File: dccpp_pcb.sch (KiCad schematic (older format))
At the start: 37 parts

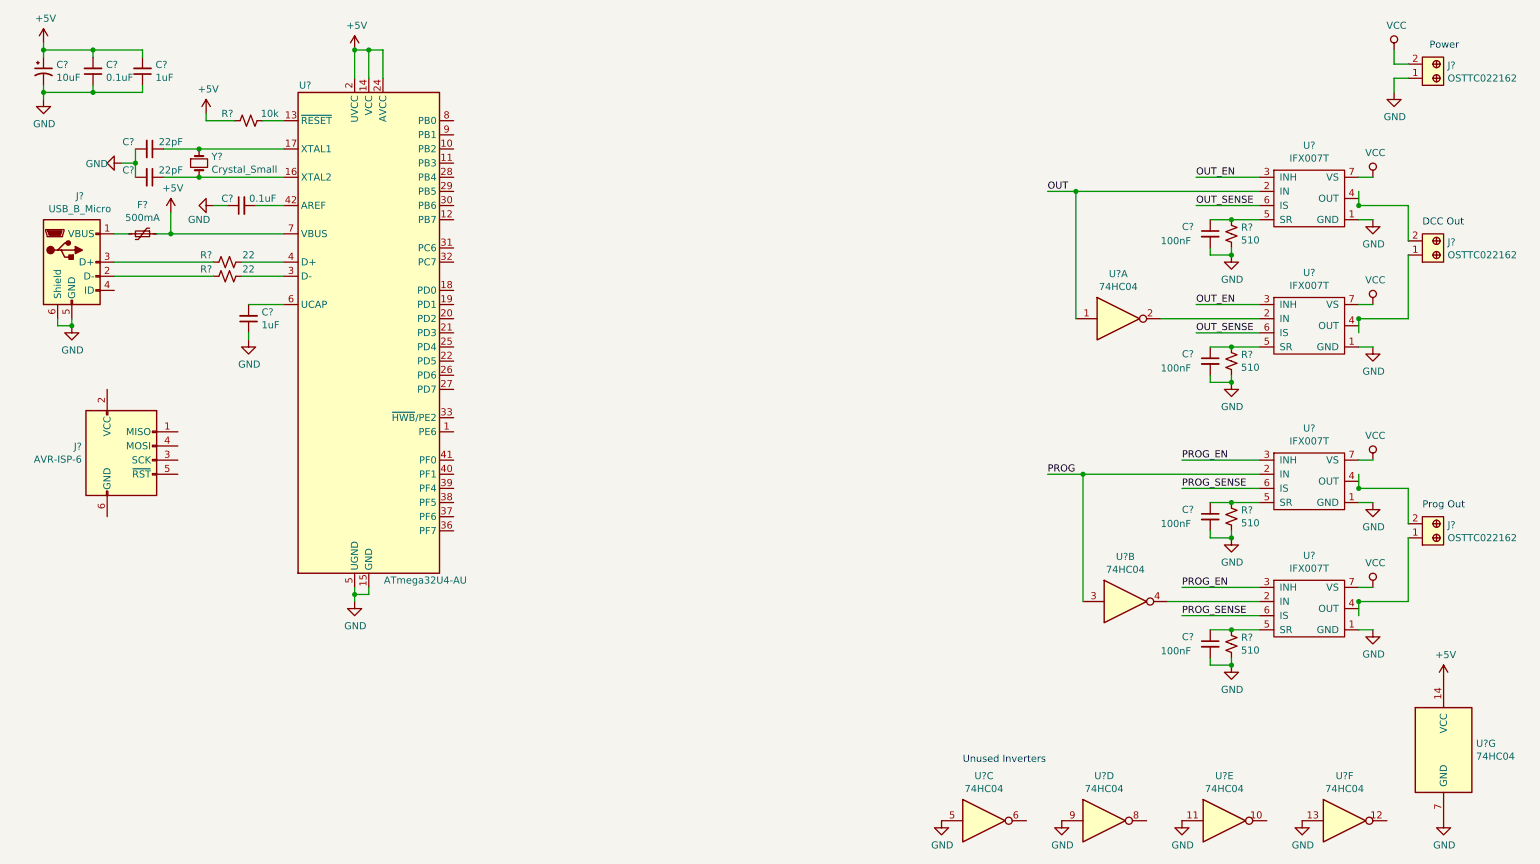
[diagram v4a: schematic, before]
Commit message: Add DCC++ pdf and current sense circuit
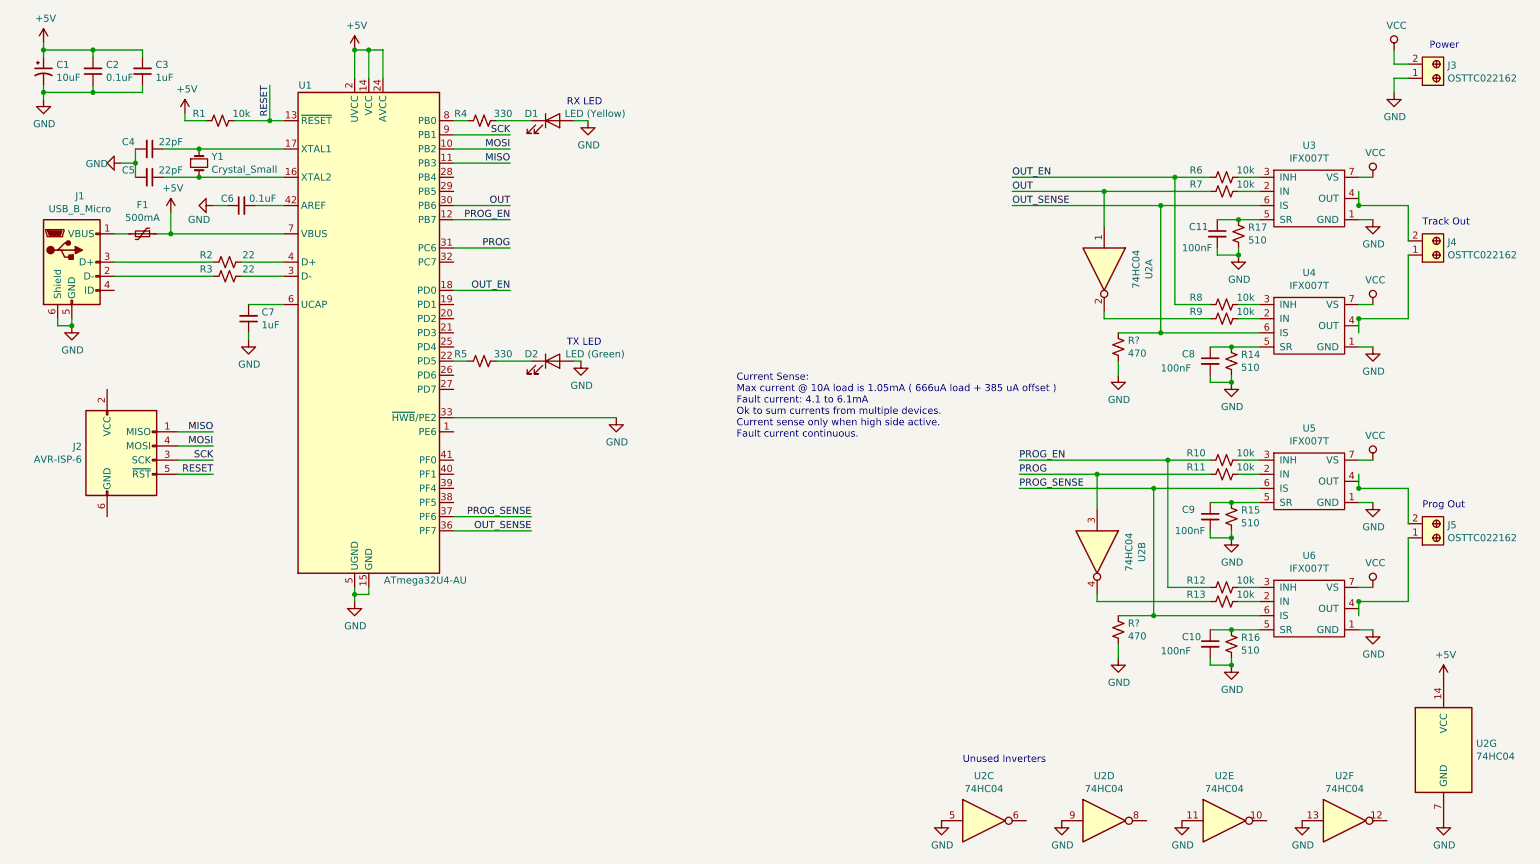
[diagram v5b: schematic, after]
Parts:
- added D1: LED (Yellow), symbol Device:LED
- added D2: LED (Green), symbol Device:LED
- added R10, R11, R12, R13, R6, R7, R8, R9: 10k, symbol Device:R_Small_US
- added R4, R5: 330, symbol Device:R_Small_US
- added R? (x2): 470, symbol Device:R_Small_US
- gave numbers to parts that had none: 31
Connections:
- net labels added: MISO, MOSI, RESET, SCK
- wire segments 106 -> 150
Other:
- note added: "Current Sense:\nMax current @ 10A load is 1.05mA ( 666uA load + 385 uA offset )\nFault current: 4.1 to 6.1mA\nOk to sum currents from multiple devices.\nCurrent sense only when high side active.\nFault current continuous."
- note added: "RX LED"
- note added: "TX LED"
- note added: "Track Out"
- note removed: "DCC Out"
- moved on the sheet: C11, R1, R17, U2A, U2B

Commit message: Fix ERC errors
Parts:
- gave numbers to parts that had none: 2
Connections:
- net +5V: now also J2.2 (VCC)
- net GND: now also J2.6 (GND)
- net D7: now reaches U1.1 (PE6)
- net D2: now reaches U1.19 (PD1)
- net D0: now reaches U1.20 (PD2)
- net D1: now reaches U1.21 (PD3)
- net D4: now reaches U1.25 (PD4)
- net D12: now reaches U1.26 (PD6)
- net D6: now reaches U1.27 (PD7)
- net D8: now reaches U1.28 (PB4)
- net D9: now reaches U1.29 (PB5)
- net D13: now reaches U1.32 (PC7)
- net A2: now reaches U1.38 (PF5)
- net A3: now reaches U1.39 (PF4)
- net A4: now reaches U1.40 (PF1)
- net A5: now reaches U1.41 (PF0)
- net at J4.1: now also U4.4 (OUT), U4.8 (OUT)
- net at J4.2: now also U3.4 (OUT), U3.8 (OUT)
- net at U5.4 (OUT), U5.8 (OUT): now also J5.2
- net at U6.4 (OUT), U6.8 (OUT): now also J5.1
- no-connect marks 0 -> 5
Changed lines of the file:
@@
 	10100 2000 10000 2000
 Wire Wire Line
-	10000 1800 10000 1900
-Wire Wire Line
-	10000 1900 10350 1900
-Connection ~ 10000 1900
-Wire Wire Line
-	10350 2250 10350 2700
-Wire Wire Line
-	10350 2700 10000 2700
-Wire Wire Line
-	10000 2700 10000 2800
-Connection ~ 10000 2700
+	10000 1850 10350 1850
+Wire Wire Line
+	10350 2250 10350 2750
+Wire Wire Line
+	10350 2750 10000 2750
 $Comp
 L dccpp:IFX007T U5
@@
 	10250 1000 10250 1100
 Wire Wire Line
-	10350 1900 10350 2150
+	10350 1850 10350 2150
 Wire Wire Line
 	10000 4900 10100 4900
@@
 	10000 3700 10100 3700
 Wire Wire Line
-	10000 3800 10000 3900
-Wire Wire Line
-	10000 3900 10350 3900
-Wire Wire Line
-	10350 3900 10350 4150
-Connection ~ 10000 3900
-Wire Wire Line
-	10350 4250 10350 4700
-Wire Wire Line
-	10350 4700 10000 4700
-Wire Wire Line
-	10000 4700 10000 4800
-Connection ~ 10000 4700
+	10000 3850 10350 3850
+Wire Wire Line
+	10350 3850 10350 4150
+Wire Wire Line
+	10350 4250 10350 4750
+Wire Wire Line
+	10350 4750 10000 4750
 Text Notes 10450 4050 0    50   ~ 0
 Prog Out
@@
 Current Sense:\nMax current @ 10A load is 1.05mA ( 666uA load + 385 uA offset )\nFault current: 4.1 to 6.1mA\nOk to sum currents from multiple devices.\nCurrent sense only when high side active.\nFault current continuous.
 $Comp
-L Device:R_Small_US R?
+L Device:R_Small_US R19
 U 1 1 5D3AA9FD
 P 8300 4900
-F 0 "R?" H 8368 4946 50  0000 L CNN
+F 0 "R19" H 8368 4946 50  0000 L CNN
 F 1 "470" H 8368 4855 50  0000 L CNN
 F 2 "" H 8300 4900 50  0001 C CNN
@@
 $EndComp
 $Comp
-L Device:R_Small_US R?
+L Device:R_Small_US R18
 U 1 1 5D3AB504
 P 8300 2900
-F 0 "R?" H 8368 2946 50  0000 L CNN
+F 0 "R18" H 8368 2946 50  0000 L CNN
 F 1 "470" H 8368 2855 50  0000 L CNN
 F 2 "" H 8300 2900 50  0001 C CNN
@@
 $EndComp
 $Comp
-L power:GND #PWR?
+L power:GND #PWR0134
 U 1 1 5D3B2373
 P 8300 3100
-F 0 "#PWR?" H 8300 2850 50  0001 C CNN
+F 0 "#PWR0134" H 8300 2850 50  0001 C CNN
 F 1 "GND" H 8305 2927 50  0000 C CNN
 F 2 "" H 8300 3100 50  0001 C CNN
@@
 $EndComp
 $Comp
-L power:GND #PWR?
+L power:GND #PWR0135
 U 1 1 5D3B27C2
 P 8300 5100
-F 0 "#PWR?" H 8300 4850 50  0001 C CNN
+F 0 "#PWR0135" H 8300 4850 50  0001 C CNN
 F 1 "GND" H 8305 4927 50  0000 C CNN
 F 2 "" H 8300 5100 50  0001 C CNN
@@
 Wire Wire Line
 	8300 5100 8300 5000
+$Comp
+L power:+5V #PWR0136
+U 1 1 5D3F86B0
+P 1150 3200
+F 0 "#PWR0136" H 1150 3050 50  0001 C CNN
+F 1 "+5V" H 1165 3373 50  0000 C CNN
+F 2 "" H 1150 3200 50  0001 C CNN
+F 3 "" H 1150 3200 50  0001 C CNN
+	1    1150 3200
+	1    0    0    -1
+$EndComp
+$Comp
+L power:GND #PWR0137
+U 1 1 5D3F8F1D
+P 1150 4100
+F 0 "#PWR0137" H 1150 3850 50  0001 C CNN
+F 1 "GND" H 1155 3927 50  0000 C CNN
+F 2 "" H 1150 4100 50  0001 C CNN
+F 3 "" H 1150 4100 50  0001 C CNN
+	1    1150 4100
+	1    0    0    -1
+$EndComp
+NoConn ~ 7650 6250
+NoConn ~ 8500 6250
+NoConn ~ 9350 6250
+NoConn ~ 10200 6250
+NoConn ~ 1200 2500
+Text Label 4000 2700 2    50   ~ 0
+D0
+Text Label 4000 2800 2    50   ~ 0
+D1
+Text Label 4000 2600 2    50   ~ 0
+D2
+Text Label 4000 2900 2    50   ~ 0
+D4
+Text Label 4000 3200 2    50   ~ 0
+D6
+Text Label 4000 3500 2    50   ~ 0
+D7
+Text Label 4000 1700 2    50   ~ 0
+D8
+Text Label 4000 1800 2    50   ~ 0
+D9
+Text Label 4000 3100 2    50   ~ 0
+D12
+Text Label 4150 4000 2    50   ~ 0
+A2
+Text Label 4150 3900 2    50   ~ 0
+A3
+Text Label 4150 3800 2    50   ~ 0
+A4
+Text Label 4150 3700 2    50   ~ 0
+A5
+Wire Wire Line
+	4150 3700 3600 3700
+Wire Wire Line
+	3600 3800 4150 3800
+Wire Wire Line
+	4150 3900 3600 3900
+Wire Wire Line
+	4150 4000 3600 4000
+Wire Wire Line
+	4000 3500 3600 3500
+Wire Wire Line
+	3600 3200 4000 3200
+Wire Wire Line
+	4000 3100 3600 3100
+Wire Wire Line
+	3600 2900 4000 2900
+Wire Wire Line
+	4000 2800 3600 2800
+Wire Wire Line
+	3600 2700 4000 2700
+Wire Wire Line
+	4000 2600 3600 2600
+Wire Wire Line
+	3600 1800 4000 1800
+Wire Wire Line
+	4000 1700 3600 1700
+Text Label 4000 2300 2    50   ~ 0
+D13
+Wire Wire Line
+	4000 2300 3600 2300
+$Comp
+L power:PWR_FLAG #FLG0101
+U 1 1 5D4E6B43
+P 1050 800
+F 0 "#FLG0101" H 1050 875 50  0001 C CNN
+F 1 "PWR_FLAG" H 1050 973 50  0000 C CNN
+F 2 "" H 1050 800 50  0001 C CNN
+F 3 "~" H 1050 800 50  0001 C CNN
+	1    1050 800
+	1    0    0    -1
+$EndComp
+$Comp
+L power:PWR_FLAG #FLG0103
+U 1 1 5D4EA9C3
+P 10250 900
+F 0 "#FLG0103" H 10250 975 50  0001 C CNN
+F 1 "PWR_FLAG" V 10250 1027 50  0000 L CNN
+F 2 "" H 10250 900 50  0001 C CNN
+F 3 "~" H 10250 900 50  0001 C CNN
+	1    10250 900
+	0    -1   -1   0
+$EndComp
+Connection ~ 10250 900
 $EndSCHEMATC
